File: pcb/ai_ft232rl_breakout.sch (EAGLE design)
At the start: 14 parts, among them U1 FT232RLSSOP

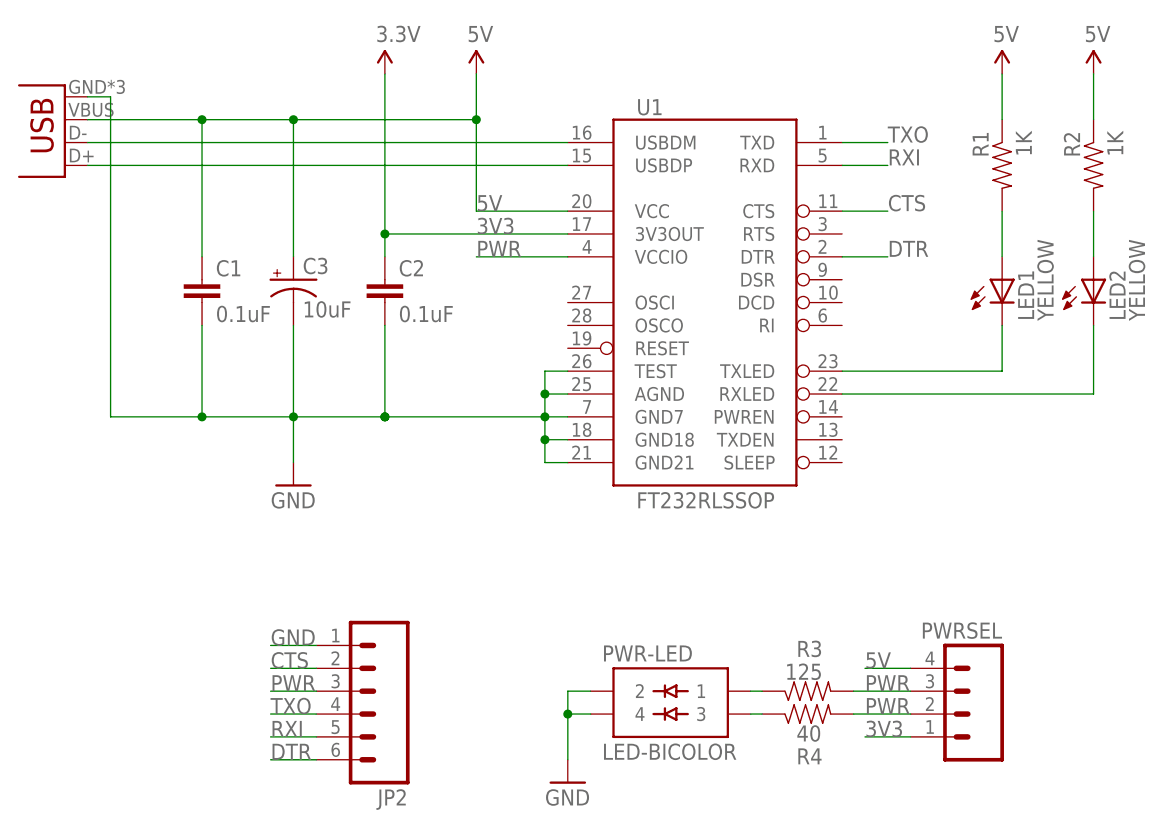
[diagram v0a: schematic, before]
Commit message: re-routed manually, and changed components to use the Ai Eagle libraries.
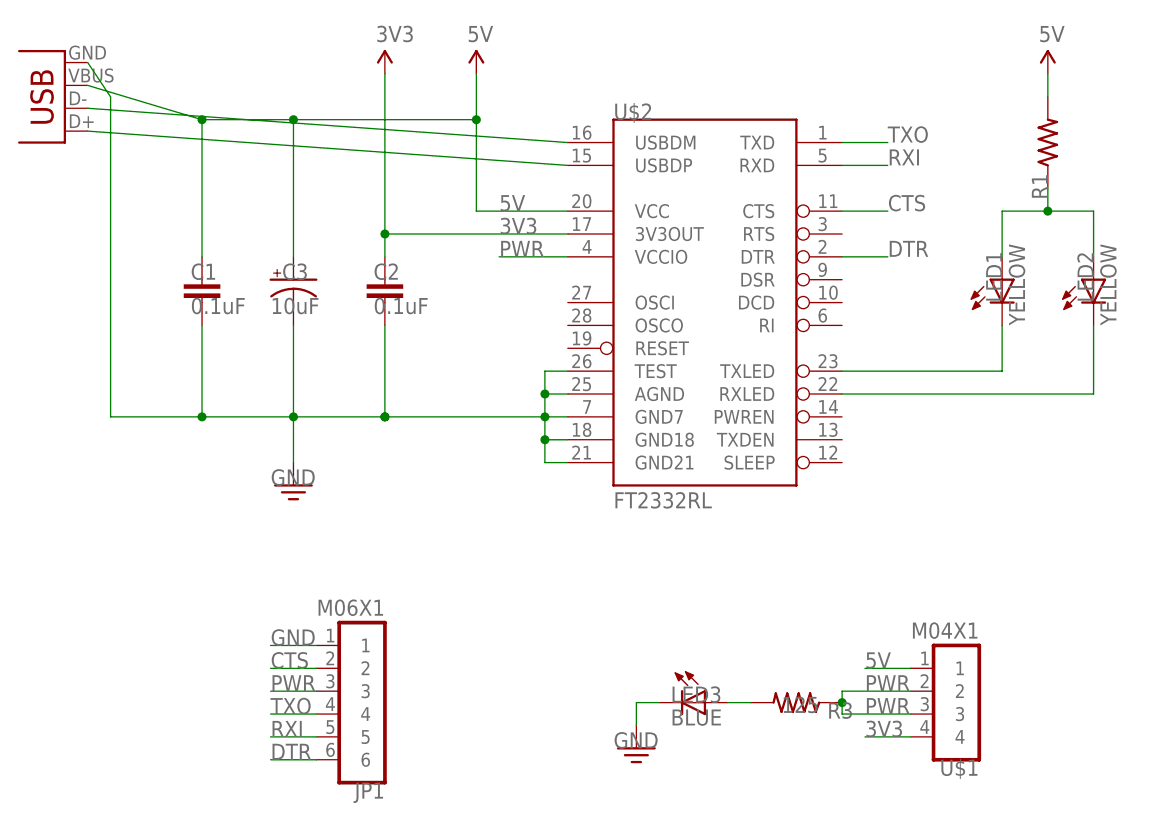
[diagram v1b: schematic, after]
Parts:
- removed JP2: (no value), SparkFun-Connectors:M06LONGPADS
- removed PWR-LED: LED-BICOLOR, Acrobotic-LED:LED-BICOLOR
- removed PWRSEL: (no value), SparkFun-Connectors:M04PTH
- removed R2: 1K, SparkFun-Resistors:RESISTOR0805-RES
- removed R4: 40, SparkFun-Resistors:RESISTOR0805-RES
- removed U1: FT232RLSSOP, SparkFun-DigitalIC:FT232RLSSOP
- removed USB: USB-MICROB, SparkFun-Connectors:USB-MICROB
- added JP1: M06X1, Ai_Connectors:M06X1
- added LED3: BLUE, Ai_LED:LED-0603
- added U$1: M04X1, Ai_Connectors:M04X1
- added U$2: FT2332RL, Ai_IC:FT2332RL
- added USB1: USB-MICROB, Ai_Connectors:USB-MICROB
- C1, C2: device SparkFun-Capacitors:CAP0805 -> Ai_Passives:CAP
- C3: device SparkFun-Passives:CAP_POL1206-KIT -> Ai_Passives:CAP_POL
- LED1: device SparkFun-LED:LED-RED0603 -> Ai_LED:LED-0603
- LED2: device SparkFun-LED:LED-GREEN0603 -> Ai_LED:LED-0603
- R1: value 1K -> (none); device SparkFun-Resistors:RESISTOR0805-RES -> Ai_Passives:RES
- R3: device SparkFun-Resistors:RESISTOR0805-RES -> Ai_Passives:RES
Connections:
- removed net N$11: PWR-LED.3, R4.1
- removed net N$5: LED2.A, R2.2
- removed net N$7: PWR-LED.1, R3.1
- removed net N$8: PWRSEL.3, R3.2
- new net N$9: LED3.A, R3.2
- net 3V3: now also U$1.4, U$2.3V3OUT; no longer PWRSEL.1, U1.3V3OUT
- net 5V: now also R1.2, U$1.1, U$2.VCC, USB1.VBUS; no longer PWRSEL.4, R1.1, R2.1, U1.VCC, USB.VBUS
- net CTS: now also JP1.2, U$2.CTS; no longer JP2.2, U1.CTS
- net DTR: now also JP1.6, U$2.DTR; no longer JP2.6, U1.DTR
- net GND: now also JP1.1, LED3.C, U$2.AGND, U$2.GND18, U$2.GND21, U$2.GND7, U$2.TEST, USB1.GND; no longer JP2.1, PWR-LED.2, PWR-LED.4, U1.AGND, U1.GND18, U1.GND21, U1.GND7, U1.TEST, USB.GND
- net N$1: now also U$2.TXLED; no longer U1.TXLED
- net N$2: now also U$2.RXLED; no longer U1.RXLED
- net N$3: now also U$2.USBDM, USB1.D-; no longer U1.USBDM, USB.D-
- net N$4: now also U$2.USBDP, USB1.D+; no longer U1.USBDP, USB.D+
- net N$6: now also LED2.A, R1.1; no longer R1.2
- net PWR: now also JP1.3, R3.1, U$1.2, U$1.3, U$2.VCCIO; no longer JP2.3, PWRSEL.2, R4.2, U1.VCCIO
- net RXI: now also JP1.5, U$2.RXD; no longer JP2.5, U1.RXD
- net TXO: now also JP1.4, U$2.TXD; no longer JP2.4, U1.TXD
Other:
- moved on the sheet: R1, R3
